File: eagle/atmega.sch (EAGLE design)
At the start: 64 parts, among them IC1 TO 5V, IC2 LM339D, Q2 16MHz, U1 ATMEGA328P-AU

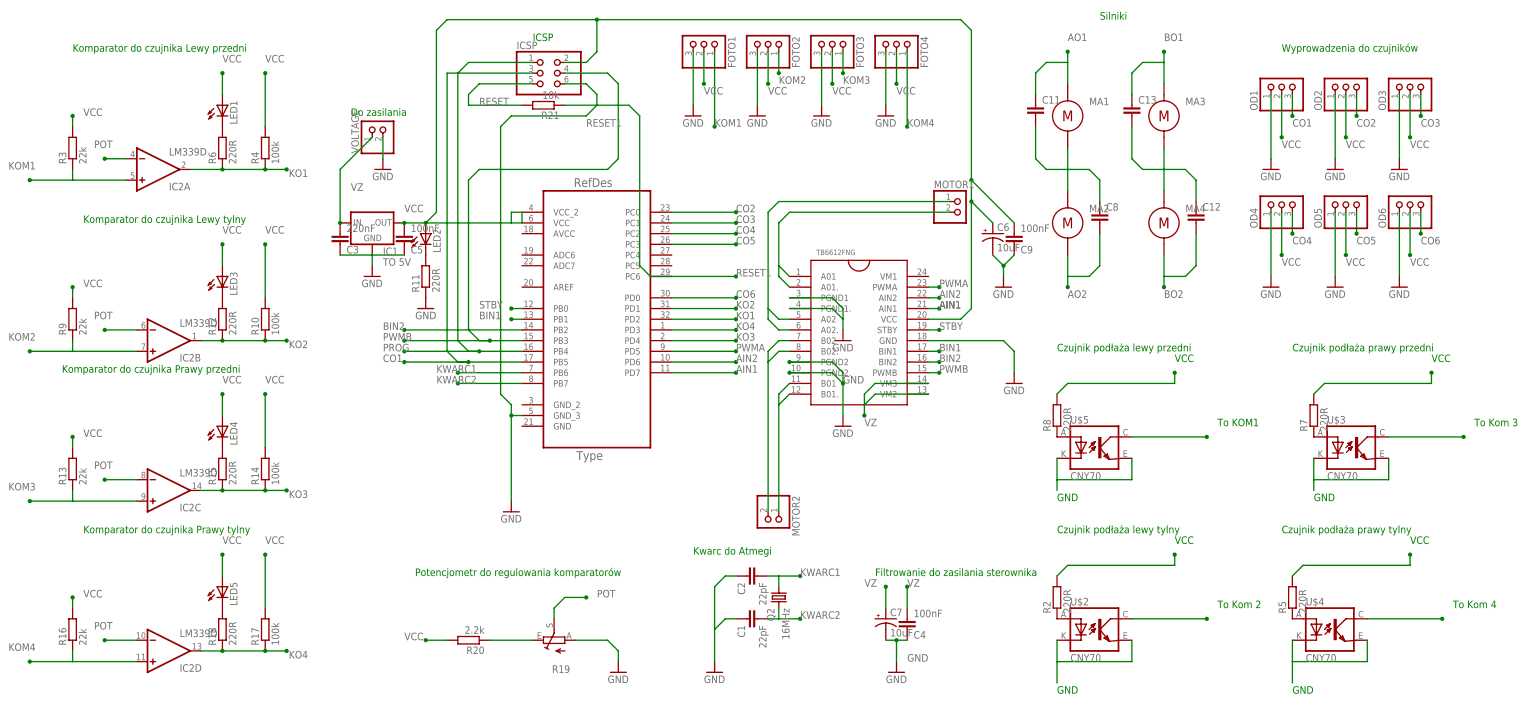
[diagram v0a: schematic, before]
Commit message: poprawnienie płytki
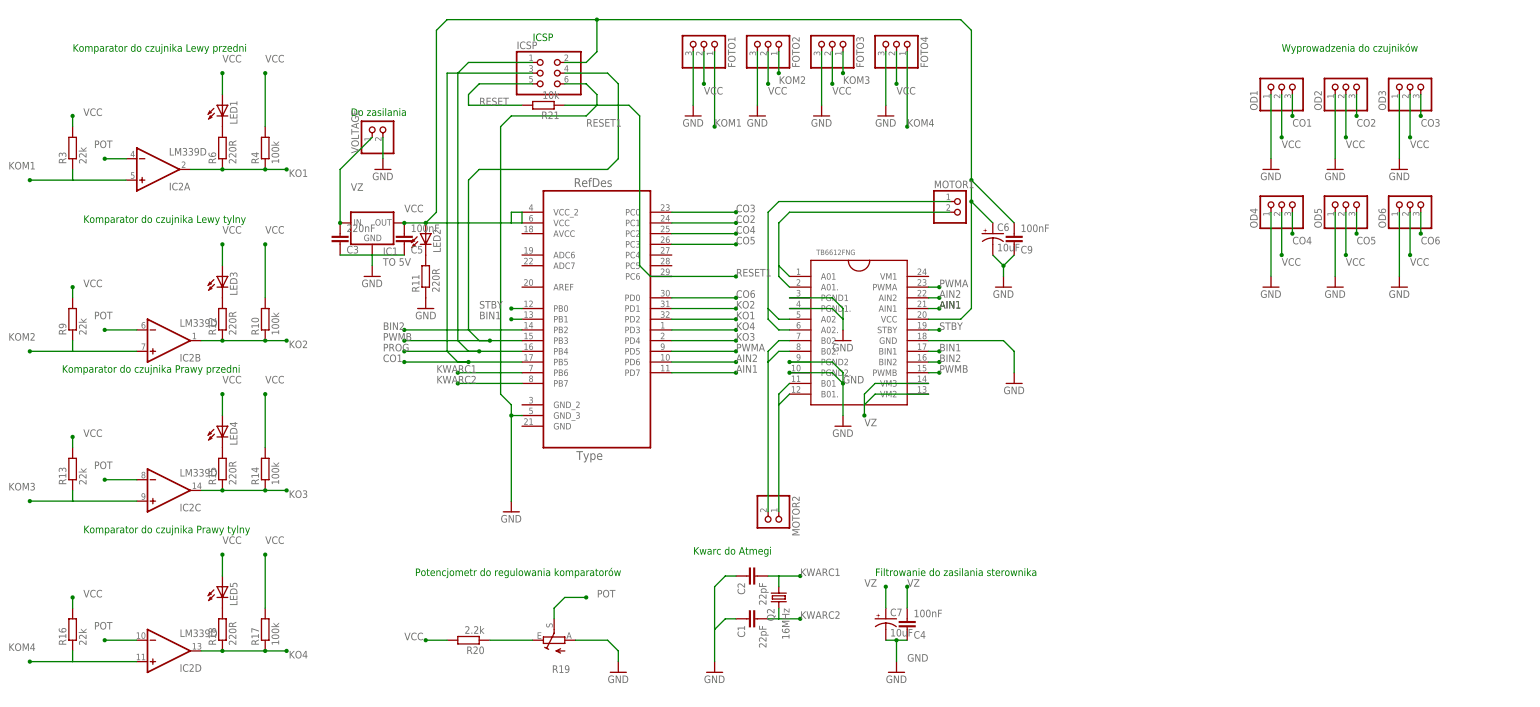
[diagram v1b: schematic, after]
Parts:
- removed C11, C12, C13, C8: (no value), capacitor-wima:C5/2.5
- removed MA1, MA2, MA3, MA4: 308-100, motors:308-100
- removed R2, R5, R7, R8: 220R, resistor:R-EU_M0805
- removed U$2, U$3, U$4, U$5: CNY70, cny70:CNY70
- C1, C2, C3, C4, C5, C9: device capacitor-wima:C2,5-3 -> rcl:C-EUC0805
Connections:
- removed net 5: R8.2
- removed net 55: R7.2
- removed net 555: R2.2
- removed net 5555: R5.2
- removed net AO1: C11.1, MA1.POS
- removed net AO2: C8.2, MA2.NEG
- removed net BO1: C13.1, MA3.POS
- removed net BO2: C12.2, MA4.NEG
- removed net N$10: R5.1, U$4.A
- removed net N$12: U$4.C, U$4.EMI
- removed net N$14: U$3.C, U$3.EMI
- removed net N$15: U$5.C, U$5.EMI
- removed net N$23: U$3.COL
- removed net N$26: C11.2, C8.1, MA1.NEG, MA2.POS
- removed net N$28: R7.1, U$3.A
- removed net N$3: U$2.COL
- removed net N$30: U$4.COL
- removed net N$32: R8.1, U$5.A
- removed net N$36: U$5.COL
- removed net N$4: U$2.C, U$2.EMI
- removed net N$8: C12.1, C13.2, MA3.NEG, MA4.POS
- removed net N$9: R2.1, U$2.A
- net CO2: now also U1.PC1; no longer U1.PC0
- net CO3: now also U1.PC0; no longer U1.PC1
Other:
- note removed: "Czujnik podłaża lewy przedni"
- note removed: "Czujnik podłaża lewy tylny"
- note removed: "Czujnik podłaża prawy przedni"
- note removed: "Czujnik podłaża prawy tylny"
- note removed: "GND"
- note removed: "Silniki"
- note removed: "To KOM1"
- note removed: "To Kom 2"
- note removed: "To Kom 3"
- note removed: "To Kom 4"
- note removed: "VCC"

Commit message: Dopisanie kilku komentarzy do schematu
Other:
- note added: "B"
- note added: "F"
- note added: "LB"
- note added: "LF"
- note added: "RB"
- note added: "RF"
- note added: "Wyprowadzenia do czujników odległości"
- note removed: "Wyprowadzenia do czujników"
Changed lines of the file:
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@@
 <text x="-60.96" y="-35.56" size="1.778" layer="91">Potencjometr do regulowania komparatorów</text>
 <text x="-76.2" y="73.66" size="1.778" layer="91">Do zasilania</text>
-<text x="144.78" y="88.9" size="1.778" layer="91">Wyprowadzenia do czujników</text>
+<text x="139.7" y="86.36" size="1.778" layer="91">Wyprowadzenia do czujników odległości</text>
+<text x="142.24" y="83.82" size="1.778" layer="91">LF</text>
+<text x="157.48" y="83.82" size="1.778" layer="91">F</text>
+<text x="172.72" y="83.82" size="1.778" layer="91">RF</text>
+<text x="142.24" y="55.88" size="1.778" layer="91">LB</text>
+<text x="157.48" y="55.88" size="1.778" layer="91">B</text>
+<text x="172.72" y="55.88" size="1.778" layer="91">RB</text>
 </plain>
 <instances>

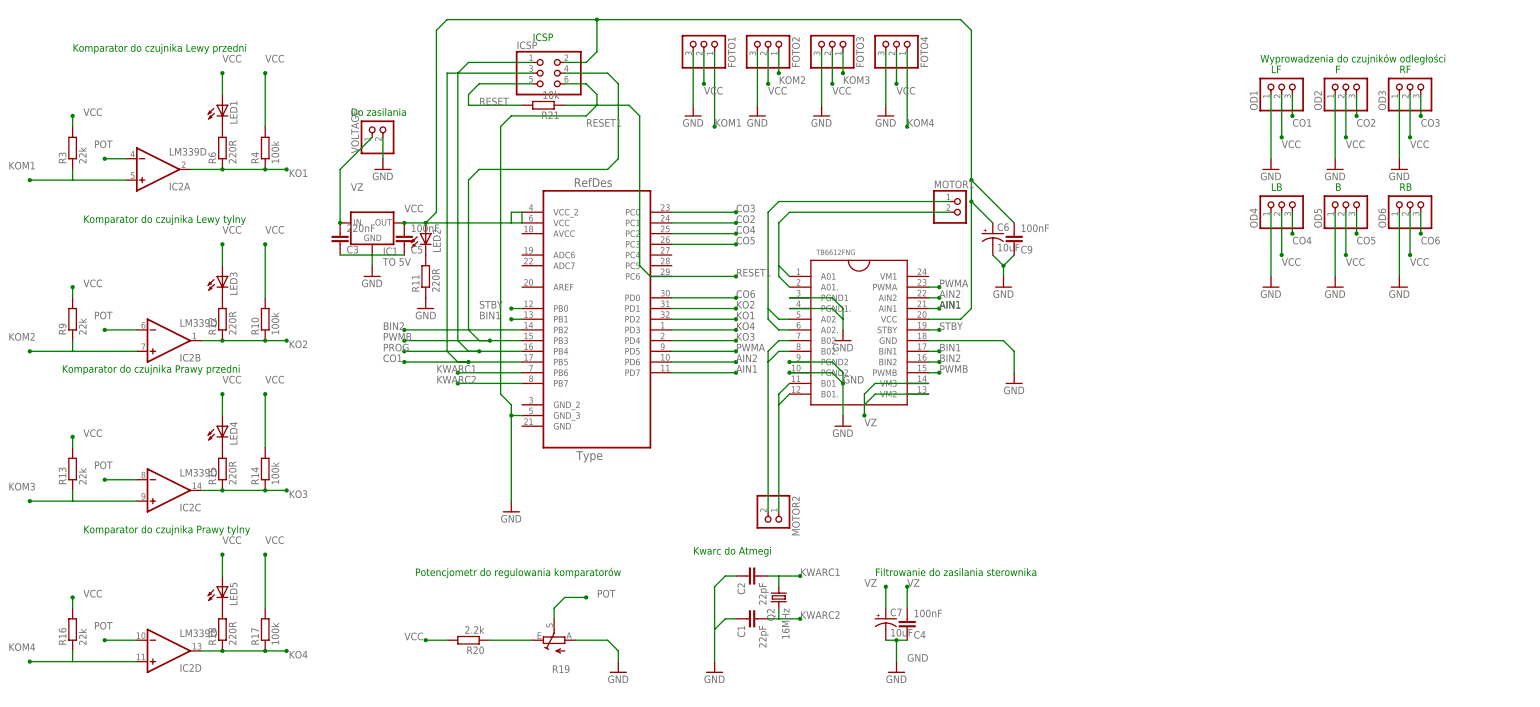
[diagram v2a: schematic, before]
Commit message: usunięcie LEDów
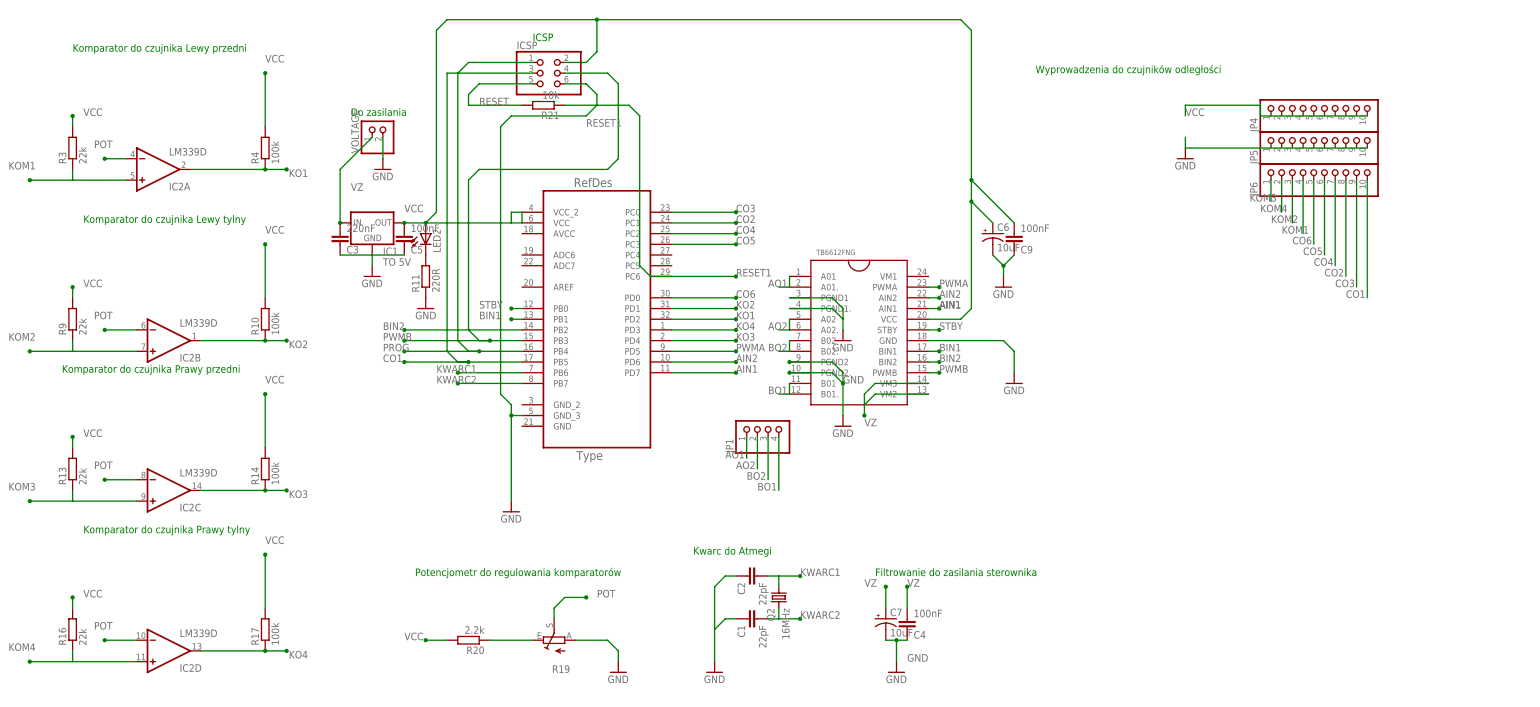
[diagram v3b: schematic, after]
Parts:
- removed FOTO1, FOTO2, FOTO3, FOTO4, OD1, OD2, OD3, OD4, OD5, OD6: (no value), pinhead:PINHD-1X3
- removed LED1, LED3, LED4, LED5: (no value), led:LEDCHIPLED_0805
- removed MOTOR1, MOTOR2: (no value), pinhead:PINHD-1X2
- removed R12, R15, R18, R6: 220R, resistor:R-EU_M0805
- added JP1: (no value), pinhead:PINHD-1X4
- added JP4, JP5, JP6: (no value), pinhead:PINHD-1X10
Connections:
- removed net N$2: LED3.C, R12.2
- removed net N$20: LED1.C, R6.2
- removed net N$21: LED4.C, R15.2
- removed net N$29: LED5.C, R18.2
- removed net OUTMA1: MOTOR1.2, U$1.A01, U$1.A01.
- removed net OUTMA2: MOTOR1.1, U$1.A02, U$1.A02.
- removed net OUTMB1: MOTOR2.1, U$1.B01, U$1.B01.
- removed net OUTMB2: MOTOR2.2, U$1.B02, U$1.B02.
- new net AO1: JP1.1, U$1.A01, U$1.A01.
- new net AO2: JP1.2, U$1.A02, U$1.A02.
- new net BO1: JP1.4, U$1.B01, U$1.B01.
- new net BO2: JP1.3, U$1.B02, U$1.B02.
- net CO1: now also JP6.10; no longer OD1.3
- net CO2: now also JP6.8; no longer OD2.3
- net CO3: now also JP6.9; no longer OD3.3
- net CO4: now also JP6.7; no longer OD4.3
- net CO5: now also JP6.6; no longer OD5.3
- net CO6: now also JP6.5; no longer OD6.3
- net GND: now also JP5.10; no longer FOTO1.3, FOTO2.3, FOTO3.3, FOTO4.3, OD1.1, OD2.1, OD3.1, OD4.1, OD5.1, OD6.1
- net KO1: no longer R6.1
- net KO2: no longer R12.1
- net KO3: no longer R15.1
- net KO4: no longer R18.1
- net KOM1: now also JP6.4; no longer FOTO1.1
- net KOM2: now also JP6.3; no longer FOTO2.1
- net KOM3: now also JP6.1; no longer FOTO3.1
- net KOM4: now also JP6.2; no longer FOTO4.1
- net VCC: now also JP4.10; no longer FOTO1.2, FOTO2.2, FOTO3.2, FOTO4.2, LED1.A, LED3.A, LED4.A, LED5.A, OD1.2, OD2.2, OD3.2, OD4.2, OD5.2, OD6.2
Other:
- note removed: "B"
- note removed: "F"
- note removed: "LB"
- note removed: "LF"
- note removed: "RB"
- note removed: "RF"

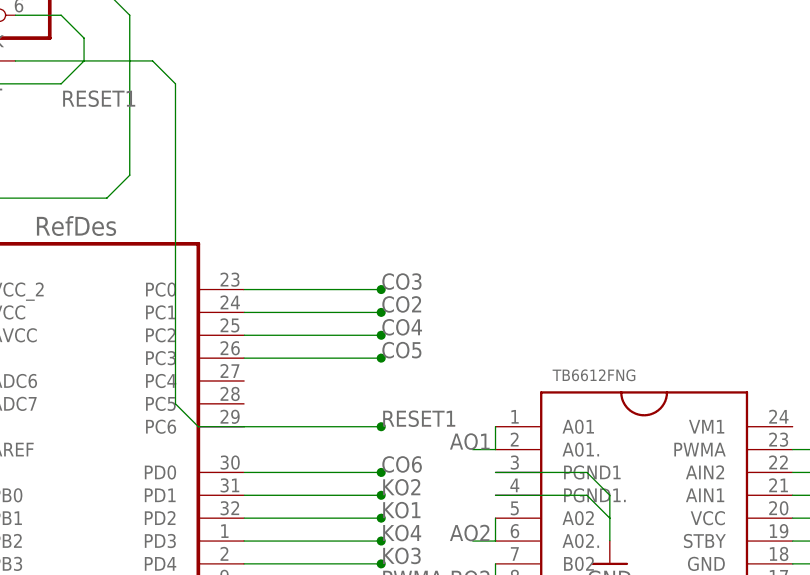
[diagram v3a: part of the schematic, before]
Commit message: Dodano zasilanie, ISCP, podłączono do tego atmege
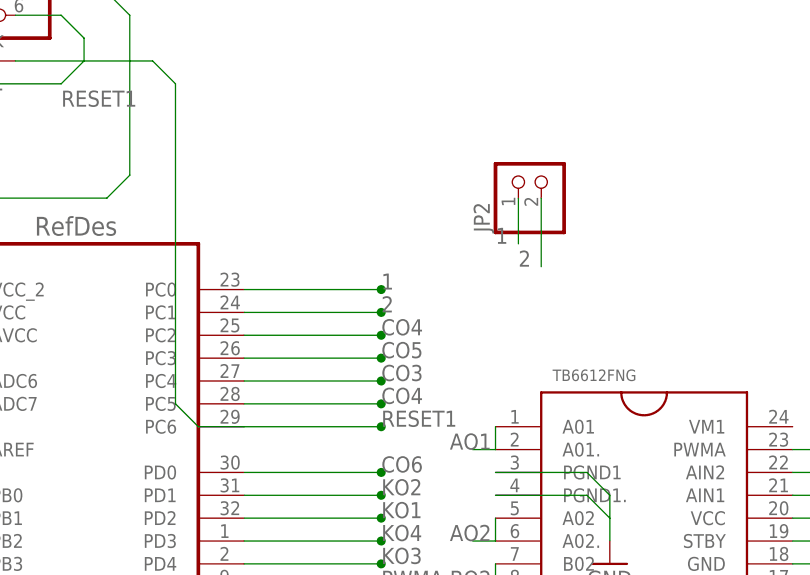
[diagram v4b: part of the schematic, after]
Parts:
- added JP2: (no value), pinhead:PINHD-1X2
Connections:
- new net 1: JP2.1, U1.PC0
- new net 2: JP2.2, U1.PC1
- net CO2: no longer U1.PC1
- net CO3: now also U1.PC4; no longer U1.PC0
- net CO4: now also U1.PC5
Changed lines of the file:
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@@
 <part name="JP6" library="pinhead" library_urn="urn:adsk.eagle:library:325" deviceset="PINHD-1X10" device="" package3d_urn="urn:adsk.eagle:package:22406/2"/>
 <part name="JP1" library="pinhead" library_urn="urn:adsk.eagle:library:325" deviceset="PINHD-1X4" device="" package3d_urn="urn:adsk.eagle:package:22407/2"/>
+<part name="JP2" library="pinhead" library_urn="urn:adsk.eagle:library:325" deviceset="PINHD-1X2" device="" package3d_urn="urn:adsk.eagle:package:22435/2"/>
 </parts>
 <sheets>
@@
 <instance part="JP6" gate="A" x="152.4" y="60.96" rot="R90"/>
 <instance part="JP1" gate="A" x="22.86" y="0" rot="R90"/>
+<instance part="JP2" gate="G$1" x="33.02" y="63.5" rot="R90"/>
 </instances>
 <busses>
@@
 <net name="CO2" class="0">
 <segment>
-<pinref part="U1" gate="A" pin="PC1"/>
-<wire x1="0" y1="48.26" x2="15.24" y2="48.26" width="0.1524" layer="91"/>
-<junction x="15.24" y="48.26"/>
-<label x="15.24" y="48.26" size="1.778" layer="95"/>
-</segment>
-<segment>
 <pinref part="JP6" gate="A" pin="8"/>
 <wire x1="160.02" y1="58.42" x2="160.02" y2="35.56" width="0.1524" layer="91"/>
@@
 <net name="CO3" class="0">
 <segment>
-<pinref part="U1" gate="A" pin="PC0"/>
-<wire x1="0" y1="50.8" x2="15.24" y2="50.8" width="0.1524" layer="91"/>
-<junction x="15.24" y="50.8"/>
-<label x="15.24" y="50.8" size="1.778" layer="95"/>
-</segment>
-<segment>
 <pinref part="JP6" gate="A" pin="9"/>
 <wire x1="162.56" y1="58.42" x2="162.56" y2="33.02" width="0.1524" layer="91"/>
 <label x="157.48" y="33.02" size="1.778" layer="95"/>
+</segment>
+<segment>
+<pinref part="U1" gate="A" pin="PC4"/>
+<wire x1="0" y1="40.64" x2="15.24" y2="40.64" width="0.1524" layer="91"/>
+<junction x="15.24" y="40.64"/>
+<label x="15.24" y="40.64" size="1.778" layer="95"/>
 </segment>
 </net>
@@
 <wire x1="157.48" y1="58.42" x2="157.48" y2="38.1" width="0.1524" layer="91"/>
 <label x="152.4" y="38.1" size="1.778" layer="95"/>
+</segment>
+<segment>
+<pinref part="U1" gate="A" pin="PC5"/>
+<wire x1="0" y1="38.1" x2="15.24" y2="38.1" width="0.1524" layer="91"/>
+<junction x="15.24" y="38.1"/>
+<label x="15.24" y="38.1" size="1.778" layer="95"/>
 </segment>
 </net>
@@
 </segment>
 </net>
+<net name="2" class="0">
+<segment>
+<pinref part="U1" gate="A" pin="PC1"/>
+<wire x1="0" y1="48.26" x2="15.24" y2="48.26" width="0.1524" layer="91"/>
+<junction x="15.24" y="48.26"/>
+<label x="15.24" y="48.26" size="1.778" layer="95"/>
+</segment>
+<segment>
+<pinref part="JP2" gate="G$1" pin="2"/>
+<wire x1="33.02" y1="60.96" x2="33.02" y2="53.34" width="0.1524" layer="91"/>
+<label x="30.48" y="53.34" size="1.778" layer="95"/>
+</segment>
+</net>
+<net name="1" class="0">
+<segment>
+<pinref part="JP2" gate="G$1" pin="1"/>
+<wire x1="30.48" y1="60.96" x2="30.48" y2="55.88" width="0.1524" layer="91"/>
+<label x="27.94" y="55.88" size="1.778" layer="95"/>
+</segment>
+<segment>
+<pinref part="U1" gate="A" pin="PC0"/>
+<wire x1="0" y1="50.8" x2="15.24" y2="50.8" width="0.1524" layer="91"/>
+<junction x="15.24" y="50.8"/>
+<label x="15.24" y="50.8" size="1.778" layer="95"/>
+</segment>
+</net>

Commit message: komparator
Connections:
- net CO2: now also U1.PC5
- net CO4: no longer U1.PC5
- net KO1: now also U1.PD1; no longer U1.PD2
- net KO2: now also U1.PD2; no longer U1.PD1
- net KO3: now also U1.PD3; no longer U1.PD4
- net KO4: now also U1.PD4; no longer U1.PD3
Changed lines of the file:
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@@
 </segment>
 <segment>
-<pinref part="U1" gate="A" pin="PD2"/>
-<wire x1="15.24" y1="25.4" x2="0" y2="25.4" width="0.1524" layer="91"/>
-<junction x="15.24" y="25.4"/>
-<label x="15.24" y="25.4" size="1.778" layer="95"/>
+<pinref part="U1" gate="A" pin="PD1"/>
+<wire x1="0" y1="27.94" x2="15.24" y2="27.94" width="0.1524" layer="91"/>
+<junction x="15.24" y="27.94"/>
+<label x="15.24" y="27.94" size="1.778" layer="95"/>
 </segment>
 </net>
@@
 </segment>
 <segment>
-<pinref part="U1" gate="A" pin="PD1"/>
-<wire x1="0" y1="27.94" x2="15.24" y2="27.94" width="0.1524" layer="91"/>
-<junction x="15.24" y="27.94"/>
-<label x="15.24" y="27.94" size="1.778" layer="95"/>
+<pinref part="U1" gate="A" pin="PD2"/>
+<wire x1="15.24" y1="25.4" x2="0" y2="25.4" width="0.1524" layer="91"/>
+<junction x="15.24" y="25.4"/>
+<label x="15.24" y="25.4" size="1.778" layer="95"/>
 </segment>
 </net>
@@
 </segment>
 <segment>
-<pinref part="U1" gate="A" pin="PD4"/>
-<wire x1="0" y1="20.32" x2="15.24" y2="20.32" width="0.1524" layer="91"/>
-<label x="15.24" y="20.32" size="1.778" layer="95"/>
-<junction x="15.24" y="20.32"/>
+<pinref part="U1" gate="A" pin="PD3"/>
+<wire x1="0" y1="22.86" x2="15.24" y2="22.86" width="0.1524" layer="91"/>
+<junction x="15.24" y="22.86"/>
+<label x="15.24" y="22.86" size="1.778" layer="95"/>
 </segment>
 </net>
@@
 </segment>
 <segment>
-<pinref part="U1" gate="A" pin="PD3"/>
-<wire x1="0" y1="22.86" x2="15.24" y2="22.86" width="0.1524" layer="91"/>
-<junction x="15.24" y="22.86"/>
-<label x="15.24" y="22.86" size="1.778" layer="95"/>
+<pinref part="U1" gate="A" pin="PD4"/>
+<wire x1="0" y1="20.32" x2="15.24" y2="20.32" width="0.1524" layer="91"/>
+<label x="15.24" y="20.32" size="1.778" layer="95"/>
+<junction x="15.24" y="20.32"/>
 </segment>
 </net>
@@
 <label x="154.94" y="35.56" size="1.778" layer="95"/>
 </segment>
+<segment>
+<pinref part="U1" gate="A" pin="PC5"/>
+<wire x1="0" y1="38.1" x2="15.24" y2="38.1" width="0.1524" layer="91"/>
+<junction x="15.24" y="38.1"/>
+<label x="15.24" y="38.1" size="1.778" layer="95"/>
+</segment>
 </net>
 <net name="CO3" class="0">
@@
 <label x="152.4" y="38.1" size="1.778" layer="95"/>
 </segment>
-<segment>
-<pinref part="U1" gate="A" pin="PC5"/>
-<wire x1="0" y1="38.1" x2="15.24" y2="38.1" width="0.1524" layer="91"/>
-<junction x="15.24" y="38.1"/>
-<label x="15.24" y="38.1" size="1.778" layer="95"/>
-</segment>
 </net>
